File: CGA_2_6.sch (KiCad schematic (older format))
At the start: 16 parts, among them U10 74153, U101 74S174, U24 74LS244, U31 74S08, U32 74LS166, U33 MK36000, U34 74LS273, U35 74LS273, U36 74LS244, U37 74LS374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

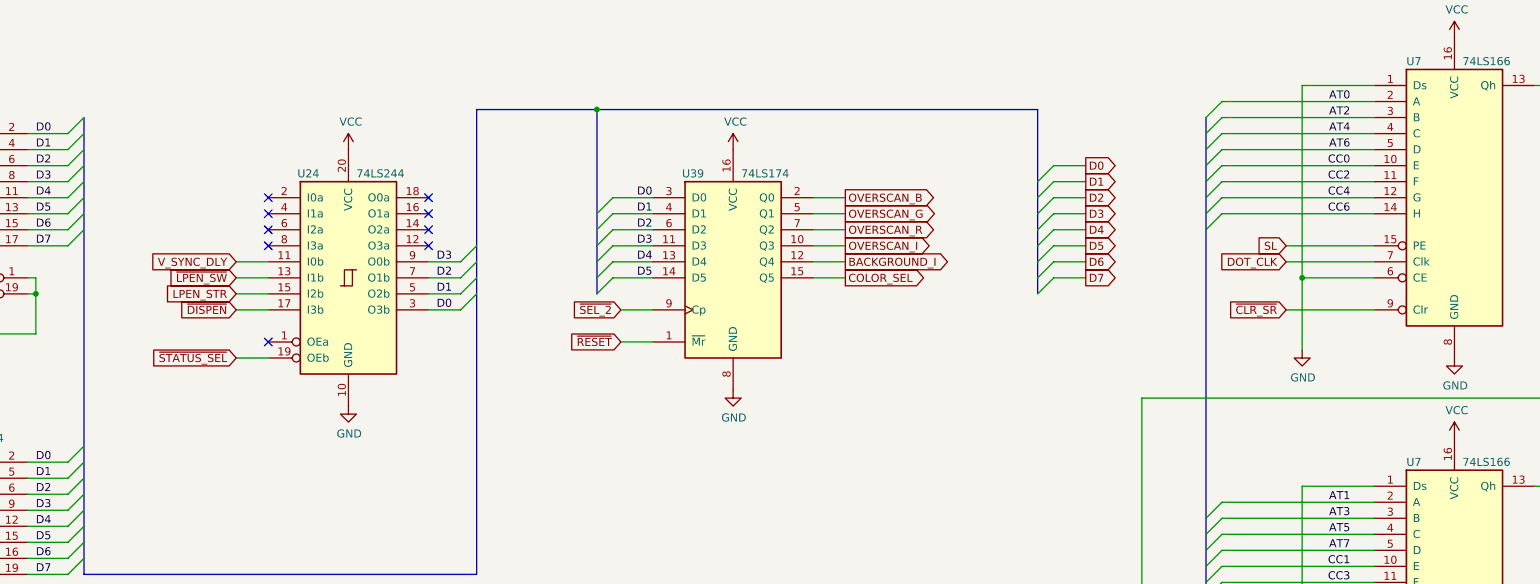
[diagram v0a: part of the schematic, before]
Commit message: Fixed some duplicate units and mislabeling
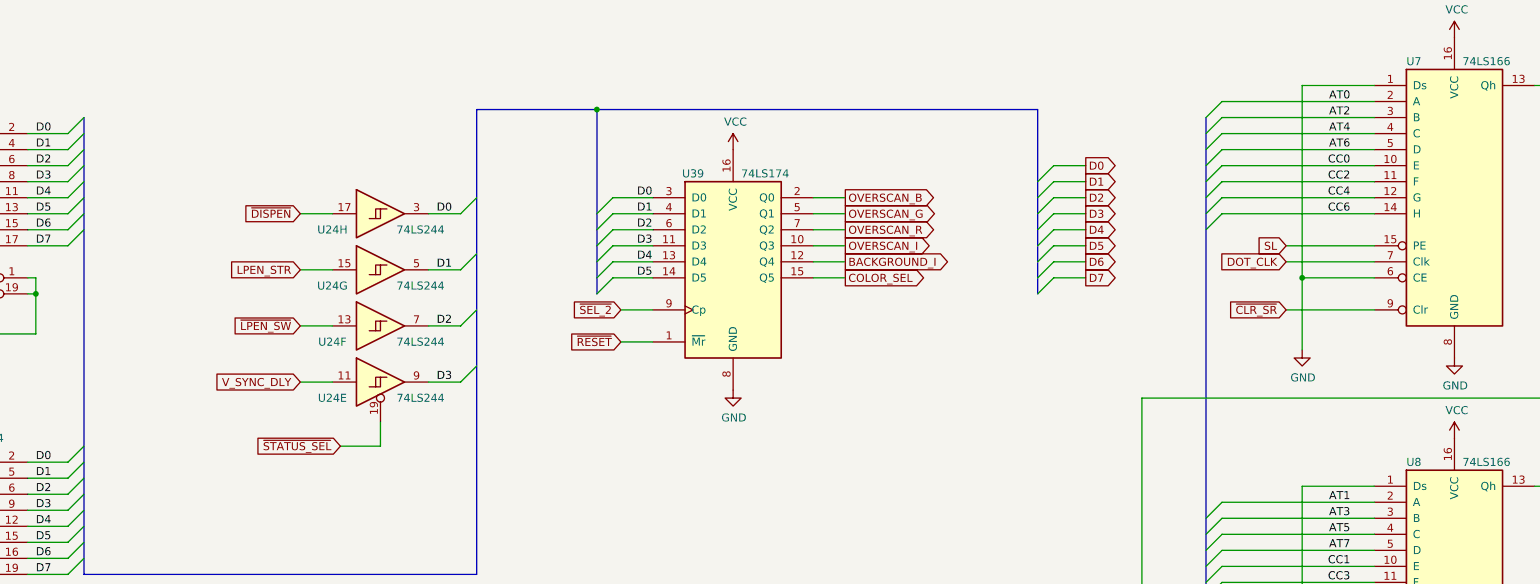
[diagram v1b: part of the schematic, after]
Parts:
- removed U24: 74LS244, Package_DIP:DIP-20_W7.62mm_LongPads, symbol 74xx:74LS244
- added U24: 74LS244, Package_DIP:DIP-20_W7.62mm_LongPads, symbol 74xx:74LS244_Split
- renumbered U7 to U8
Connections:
- net D0: now also U24.3
- net D1: now also U24.5
- net D2: now also U24.7
- net D3: now also U24.9
- net LPEN_STR: now also U24.15
- net V_SYNC_DLY: now also U24.11
- net ~DISPEN: now also U24.17
- net ~LPEN_SW: now also U24.13
- net ~STATUS_SEL: now also U24.19
- no-connect marks 9 -> 0

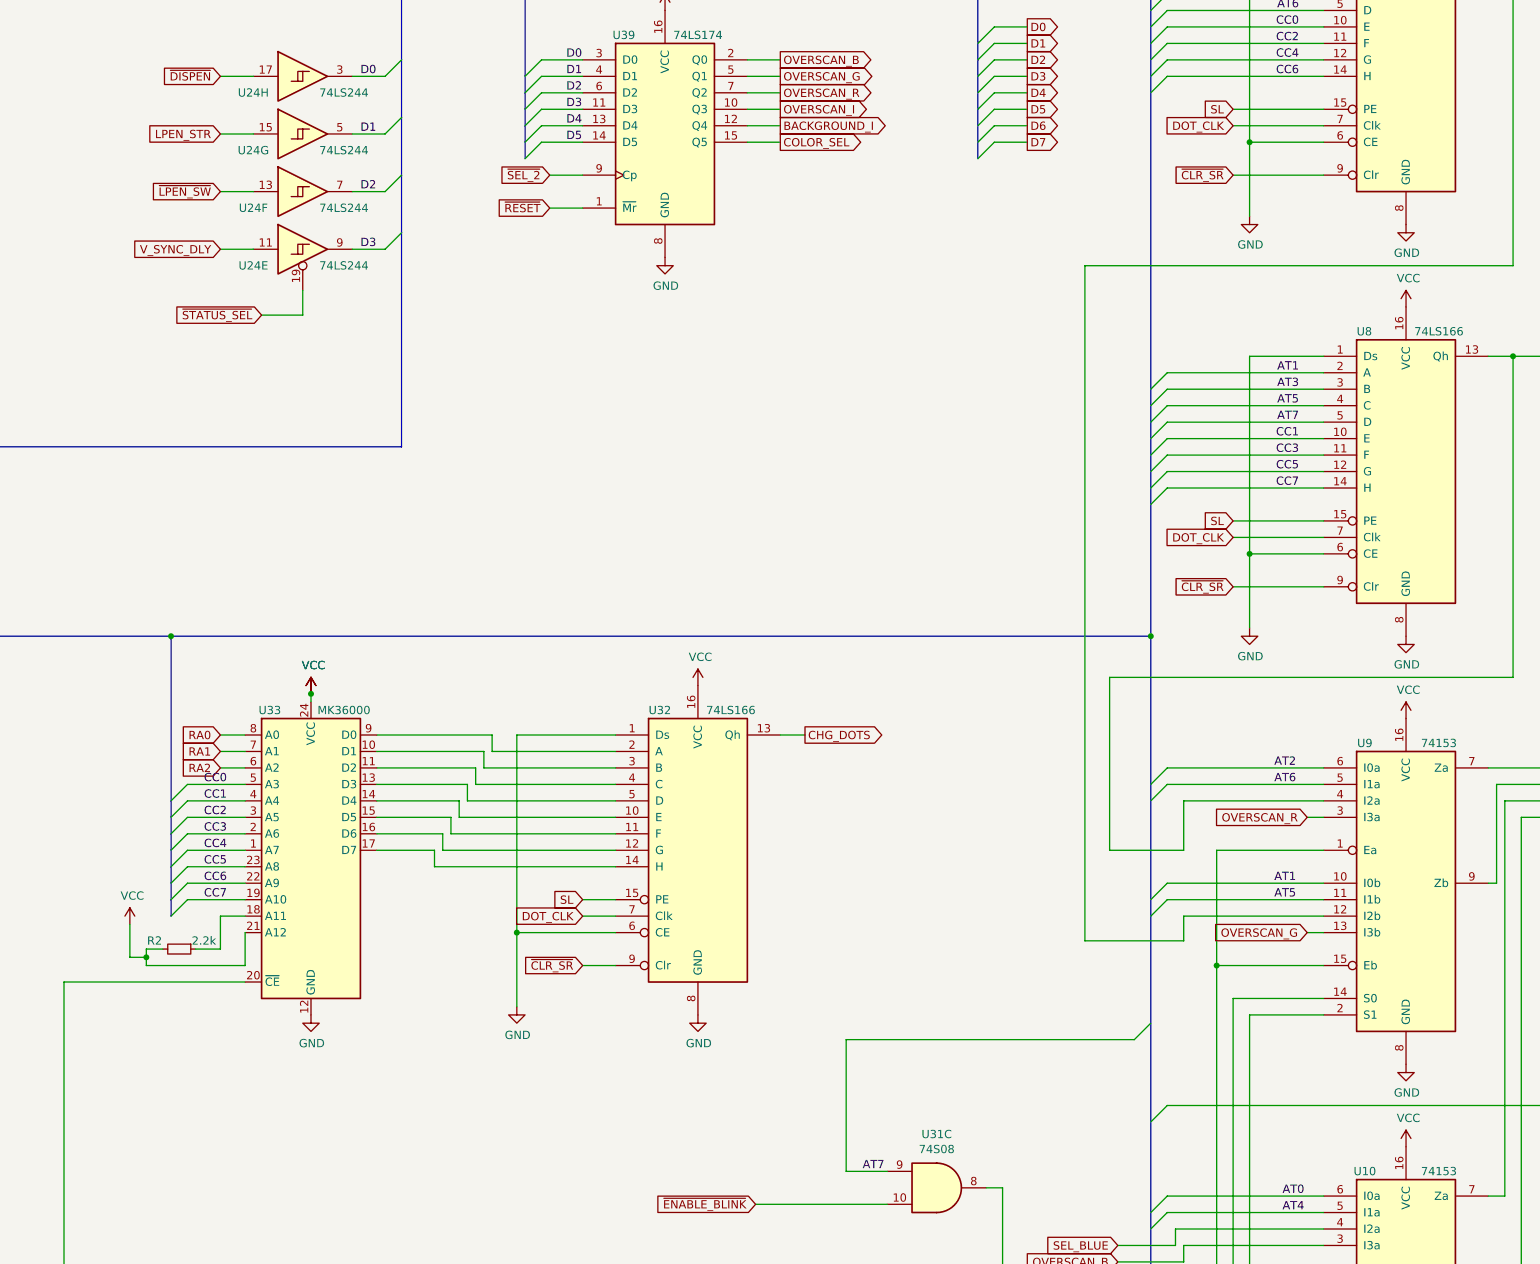
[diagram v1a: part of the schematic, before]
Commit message: Fix some more flags and footprints
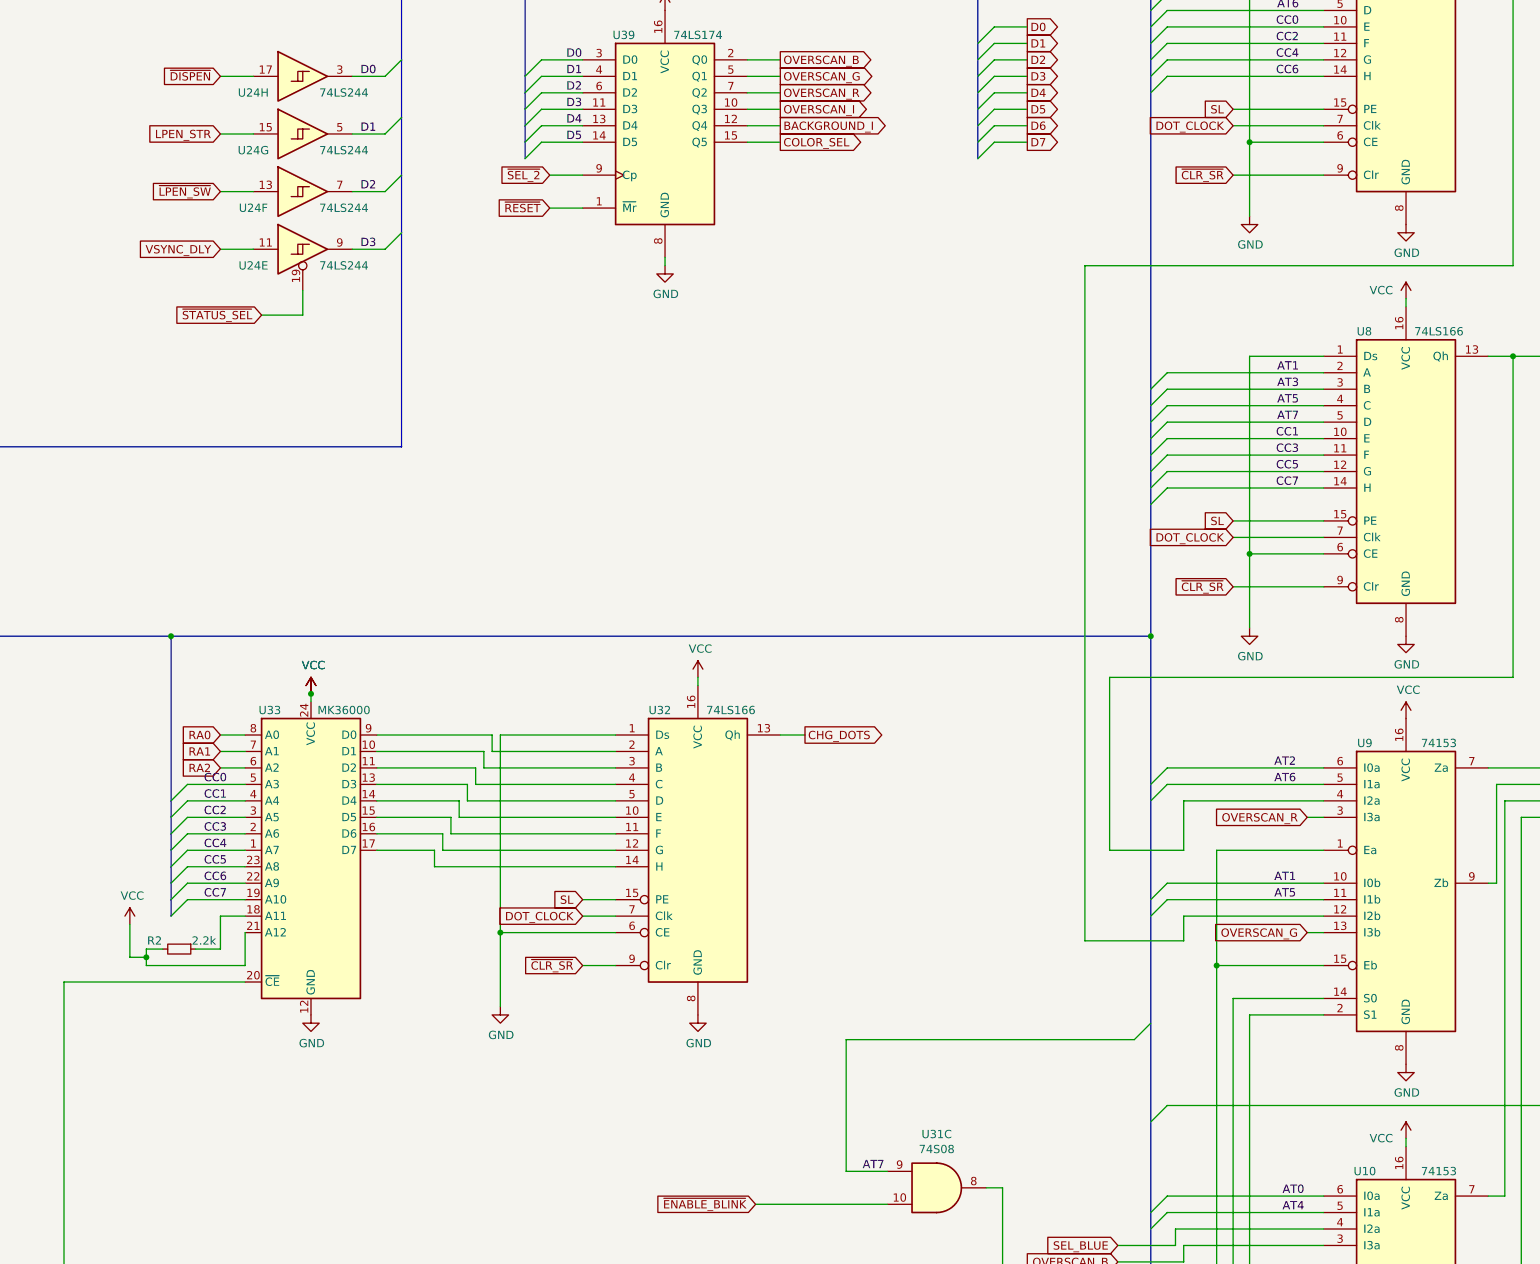
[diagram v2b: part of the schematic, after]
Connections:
- net DOT_CLK renamed DOT_CLOCK
- net V_SYNC_DLY renamed VSYNC_DLY
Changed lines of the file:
@@
 L power:VCC #PWR0138
 U 1 1 61226A83
-P 11450 8350
-F 0 "#PWR0138" H 11450 8200 50  0001 C CNN
-F 1 "VCC" H 11465 8523 50  0000 C CNN
-F 2 "" H 11450 8350 50  0001 C CNN
-F 3 "" H 11450 8350 50  0001 C CNN
-	1    11450 8350
+P 11450 8300
+F 0 "#PWR0138" H 11450 8150 50  0001 C CNN
+F 1 "VCC" H 11300 8300 50  0000 C CNN
+F 2 "" H 11450 8300 50  0001 C CNN
+F 3 "" H 11450 8300 50  0001 C CNN
+	1    11450 8300
 	1    0    0    -1
 $EndComp
@@
 	10400 4650 10950 4650
 Text GLabel 10400 4650 0    50   Input ~ 0
-DOT_CLK
+DOT_CLOCK
 Wire Wire Line
 	10400 2150 10950 2150
 Text GLabel 10400 2150 0    50   Input ~ 0
-DOT_CLK
+DOT_CLOCK
 Text GLabel 6450 6950 0    50   Input ~ 0
-DOT_CLK
+DOT_CLOCK
 Wire Wire Line
 	6450 6950 6650 6950
@@
 L power:VCC #PWR0144
 U 1 1 60E20F7C
-P 11450 3250
-F 0 "#PWR0144" H 11450 3100 50  0001 C CNN
-F 1 "VCC" H 11465 3423 50  0000 C CNN
-F 2 "" H 11450 3250 50  0001 C CNN
-F 3 "" H 11450 3250 50  0001 C CNN
-	1    11450 3250
+P 11450 3200
+F 0 "#PWR0144" H 11450 3050 50  0001 C CNN
+F 1 "VCC" H 11300 3250 50  0000 C CNN
+F 2 "" H 11450 3200 50  0001 C CNN
+F 3 "" H 11450 3200 50  0001 C CNN
+	1    11450 3200
 	1    0    0    -1
 $EndComp
@@
 	5200 6550 5550 6550
 Wire Wire Line
-	5550 6650 6650 6650
-Wire Wire Line
 	5550 6550 5550 6650
 Wire Wire Line
@@
 Wire Wire Line
 	6650 5950 5900 5950
-$Comp
-L power:GND #PWR0148
-U 1 1 60CE66D4
-P 6050 7500
-F 0 "#PWR0148" H 6050 7250 50  0001 C CNN
-F 1 "GND" H 6055 7327 50  0000 C CNN
-F 2 "" H 6050 7500 50  0001 C CNN
-F 3 "" H 6050 7500 50  0001 C CNN
-	1    6050 7500
-	1    0    0    -1
-$EndComp
-Connection ~ 6050 7050
-Wire Wire Line
-	6050 5850 6050 7050
-Wire Wire Line
-	6650 5850 6050 5850
-Wire Wire Line
-	6050 7050 6050 7500
-Wire Wire Line
-	6650 7050 6050 7050
 $Comp
 L power:VCC #PWR0149
 U 1 1 60CCD955
-P 7150 5550
-F 0 "#PWR0149" H 7150 5400 50  0001 C CNN
-F 1 "VCC" H 7165 5723 50  0000 C CNN
-F 2 "" H 7150 5550 50  0001 C CNN
-F 3 "" H 7150 5550 50  0001 C CNN
-	1    7150 5550
+P 7150 5500
+F 0 "#PWR0149" H 7150 5350 50  0001 C CNN
+F 1 "VCC" H 7165 5673 50  0000 C CNN
+F 2 "" H 7150 5500 50  0001 C CNN
+F 3 "" H 7150 5500 50  0001 C CNN
+	1    7150 5500
 	1    0    0    -1
 $EndComp
@@
 L power:GND #PWR0153
 U 1 1 609996FA
-P 6950 2950
-F 0 "#PWR0153" H 6950 2700 50  0001 C CNN
-F 1 "GND" H 6955 2777 50  0000 C CNN
-F 2 "" H 6950 2950 50  0001 C CNN
-F 3 "" H 6950 2950 50  0001 C CNN
-	1    6950 2950
+P 6950 3000
+F 0 "#PWR0153" H 6950 2750 50  0001 C CNN
+F 1 "GND" H 6955 2827 50  0000 C CNN
+F 2 "" H 6950 3000 50  0001 C CNN
+F 3 "" H 6950 3000 50  0001 C CNN
+	1    6950 3000
 	1    0    0    -1
 $EndComp
@@
 	5050 2900 5250 2900
 Text GLabel 4250 2900 0    50   Input ~ 0
-V_SYNC_DLY
+VSYNC_DLY
 Wire Wire Line
 	4450 2900 4250 2900
@@
 Entry Wire Line
 	5250 2900 5350 2800
+Wire Wire Line
+	5550 6650 6650 6650
+$Comp
+L power:GND #PWR0148
+U 1 1 60CE66D4
+P 5950 7500
+F 0 "#PWR0148" H 5950 7250 50  0001 C CNN
+F 1 "GND" H 5955 7327 50  0000 C CNN
+F 2 "" H 5950 7500 50  0001 C CNN
+F 3 "" H 5950 7500 50  0001 C CNN
+	1    5950 7500
+	1    0    0    -1
+$EndComp
+Wire Wire Line
+	5950 5850 5950 7050
+Wire Wire Line
+	5950 5850 6650 5850
+Wire Wire Line
+	5950 7050 6650 7050
+Connection ~ 5950 7050
+Wire Wire Line
+	5950 7050 5950 7500
+Wire Wire Line
+	6950 3000 6950 2950
+Wire Wire Line
+	11450 8300 11450 8350
+Wire Wire Line
+	11450 3250 11450 3200
+Wire Wire Line
+	7150 5550 7150 5500
 Wire Bus Line
 	5350 1200 5350 4100
